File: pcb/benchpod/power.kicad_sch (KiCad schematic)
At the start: 65 parts, among them J4 Screw_Terminal_01x02, J5 Screw_Terminal_01x02, J6 Screw_Terminal_01x02, U26 TPS259470ARPWR, U27 TPS259470ARPWR, U29 INA238AIDGSR, U30 TPS82130SILR, U31 AP2112K-1.2, U32 AP2112K-2.5TRG1, U33 INA238AIDGSR, U52 AP2112K-1.8TRG1, U56 TCA9554PWR

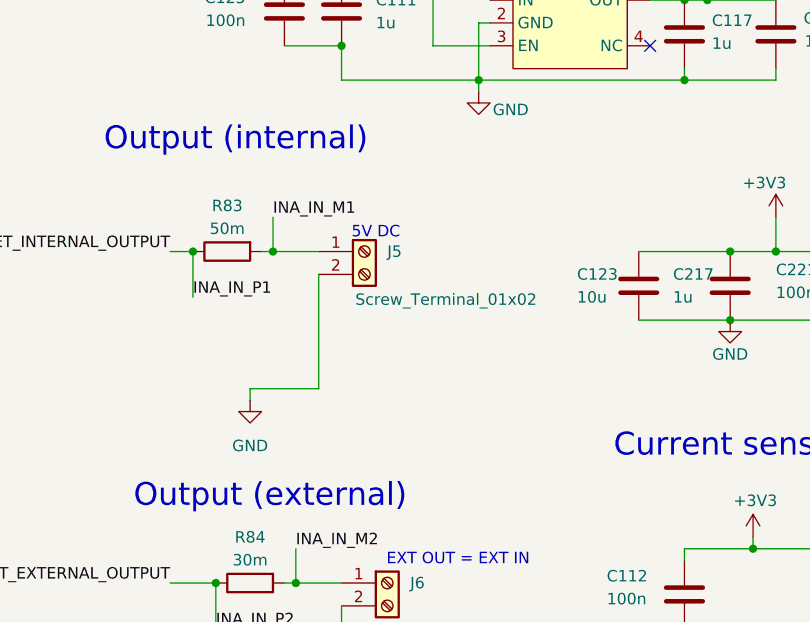
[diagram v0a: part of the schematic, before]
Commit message: expanding board, adding headers, adding usb-a
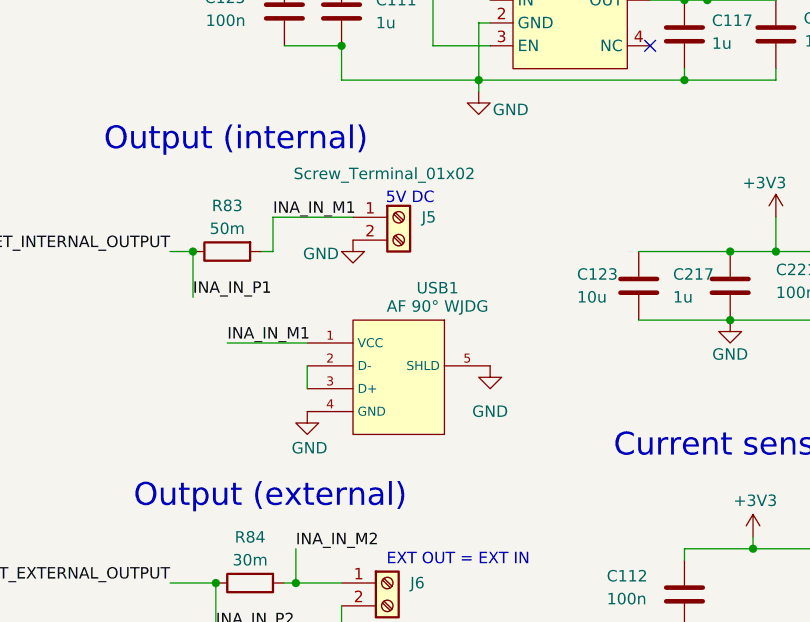
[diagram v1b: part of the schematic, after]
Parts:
- added USB1: AF 90° WJDG, lcsc_footprints:C456018_USB-A-TH_AF-WJDG, symbol lcsc_plugin:AF_90°_WJDG
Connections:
- net GND: now also USB1.4 (GND), USB1.5 (SHLD)
- net INA_IN_M1: now also USB1.1 (VCC)
- new net: USB1.2 (D-), USB1.3 (D+)
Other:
- moved on the sheet: J5

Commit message: fix pull-downs for board boot-up
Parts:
- R69, R72: value 100k -> 10k
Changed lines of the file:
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@@
 			)
 		)
-		(property "Value" "100k"
+		(property "Value" "10k"
 			(at 21.336 92.202 0)
 			(show_name no)
@@
 			)
 		)
-		(property "Value" "100k"
+		(property "Value" "10k"
 			(at 30.48 142.494 0)
 			(show_name no)

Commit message: route cleanups and out of stock component replacement
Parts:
- C108: footprint Capacitor_SMD:C_0603_1608Metric -> Capacitor_SMD:C_0805_2012Metric; LCSC C59461 -> C45783
- R69, R72: LCSC C25741 -> C25744
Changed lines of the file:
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@@
 			)
 		)
-		(property "Footprint" "Capacitor_SMD:C_0603_1608Metric"
+		(property "Footprint" "Capacitor_SMD:C_0805_2012Metric"
 			(at 192.0748 44.45 0)
 			(hide yes)
@@
 			)
 		)
-		(property "LCSC" "C59461"
+		(property "LCSC" "C45783"
 			(at 193.04 48.26 0)
 			(hide yes)
@@
 			)
 		)
-		(property "LCSC" "C25741"
+		(property "LCSC" "C25744"
 			(at 25.4 92.71 0)
 			(hide yes)
@@
 			)
 		)
-		(property "LCSC" "C25741"
+		(property "LCSC" "C25744"
 			(at 34.29 143.51 0)
 			(hide yes)

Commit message: replace d1, cleanups, cap changes
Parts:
- removed C103, C97: 10u, Capacitor_SMD:C_0603_1608Metric, symbol Device:C
- removed D5: SMAJ22A_C41376403, lcsc:SMA_L4.3-W2.6-LS5.0-RD, symbol lcsc_lib:SMAJ22A_C41376403
- added C256: 100n, Capacitor_SMD:C_0402_1005Metric, symbol Device:C
- added C257: 10u, Capacitor_SMD:C_0603_1608Metric, symbol Device:C
- added C62, C63, C64, C65: 4.7u, Capacitor_SMD:C_0805_2012Metric, symbol Device:C
- added D5: SMAJ20A, lcsc_footprints:C41376408_SMA_L4_3-W2_6-LS5_2-RD, symbol lcsc_imported:SMAJ20A_C41376408
- R71: value 100k -> 105k; LCSC C25741 -> C25742
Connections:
- net GND: now also C256.1, C257.2, C62.2, C63.2, C64.2, C65.2, D5.2
- net INA_IN_M1: now also C256.2, C257.1
- net INA_IN_P2: now also C64.1, C65.1
- net at C96.2, J4.1 (Pin_1), R70.1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: now also C62.1, C63.1, D5.1

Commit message: digital and analog cleanup
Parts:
- R83: value 50m -> 30m; LCSC C5200068 -> C2941066
- R84: value 30m -> 20m; LCSC C2941066 -> C915979
- U29, U33: value INA238AIDGSR -> INA226; LCSC C2868250 -> C49851; LCSC Part C2868250 -> C49851; MPN INA238AIDGSR -> (none); Manufacturer TI(德州仪器) -> (none)
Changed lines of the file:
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@@
 			)
 		)
-		(property "Value" "INA238AIDGSR"
+		(property "Value" "INA226"
 			(at 259.08 140.97 0)
 			(show_name no)
@@
 			)
 		)
-		(property "Datasheet" "https://www.lcsc.com/datasheet/C2868250.pdf"
+		(property "Datasheet" "https://www.lcsc.com/datasheet/C49851.pdf"
 			(at 259.08 166.37 0)
 			(hide yes)
@@
 			)
 		)
-		(property "Manufacturer" "TI(德州仪器)"
-			(at 259.08 168.91 0)
-			(hide yes)
-			(show_name no)
-			(do_not_autoplace no)
-			(effects
-				(font
-					(size 1.27 1.27)
-				)
-			)
-		)
-		(property "MPN" "INA238AIDGSR"
-			(at 259.08 171.45 0)
-			(hide yes)
-			(show_name no)
-			(do_not_autoplace no)
-			(effects
-				(font
-					(size 1.27 1.27)
-				)
-			)
-		)
-		(property "LCSC Part" "C2868250"
+		(property "LCSC Part" "C49851"
 			(at 259.08 173.99 0)
 			(hide yes)
@@
 			)
 		)
-		(property "LCSC" "C2868250"
+		(property "LCSC" "C49851"
 			(at 259.08 151.13 0)
 			(hide yes)
@@
 			)
 		)
-		(property "Value" "30m"
+		(property "Value" "20m"
 			(at 163.83 127 90)
 			(show_name no)
@@
 			)
 		)
-		(property "LCSC" "C2941066"
+		(property "LCSC" "C915979"
 			(at 163.83 129.54 90)
 			(hide yes)
@@
 			)
 		)
-		(property "Value" "50m"
+		(property "Value" "30m"
 			(at 161.29 90.17 90)
 			(show_name no)
@@
 			)
 		)
-		(property "LCSC" "C5200068"
+		(property "LCSC" "C2941066"
 			(at 161.29 92.71 90)
 			(hide yes)
@@
 			)
 		)
-		(property "Value" "INA238AIDGSR"
+		(property "Value" "INA226"
 			(at 207.01 142.24 0)
 			(show_name no)
@@
 			)
 		)
-		(property "Datasheet" "https://www.lcsc.com/datasheet/C2868250.pdf"
+		(property "Datasheet" "https://www.lcsc.com/datasheet/C49851.pdf"
 			(at 207.01 167.64 0)
 			(hide yes)
@@
 			)
 		)
-		(property "Manufacturer" "TI(德州仪器)"
-			(at 207.01 170.18 0)
-			(hide yes)
-			(show_name no)
-			(do_not_autoplace no)
-			(effects
-				(font
-					(size 1.27 1.27)
-				)
-			)
-		)
-		(property "MPN" "INA238AIDGSR"
-			(at 207.01 172.72 0)
-			(hide yes)
-			(show_name no)
-			(do_not_autoplace no)
-			(effects
-				(font
-					(size 1.27 1.27)
-				)
-			)
-		)
-		(property "LCSC Part" "C2868250"
+		(property "LCSC Part" "C49851"
 			(at 207.01 175.26 0)
 			(hide yes)
@@
 			)
 		)
-		(property "LCSC" "C2868250"
+		(property "LCSC" "C49851"
 			(at 207.01 152.4 0)
 			(hide yes)

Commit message: Benchpod v3.0.1 work (#1)
* bom replacements and footprint replacements for out of stock items

* replacements and fixes

* smaller fixes

* finalized v3r1

* finshunt work on digital (wip)
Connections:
- net +5V: no longer C94.2, C95.1, R67.1, U26.5 (IN)
- new net +5V_IN: C94.2, C95.1, R67.1, U26.5 (IN)
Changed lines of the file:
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@@
 			)
 		)
-		(property "Value" "+5V"
+		(property "Value" "+5V_IN"
 			(at 13.97 96.012 0)
 			(show_name no)
